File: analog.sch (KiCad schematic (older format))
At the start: 8 parts, among them J18 A3, J19 A4

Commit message: Added images Added information to schematic Added information to layout
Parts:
- renumbered C25 to C21, C26 to C22, J18 to J14, J19 to J15
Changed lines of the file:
@@
 encoding utf-8
 Sheet 8 11
-Title ""
-Date ""
-Rev ""
-Comp ""
-Comment1 ""
+Title "AirMon"
+Date "2020-01-13"
+Rev "0.1"
+Comp "Jörg Bayer"
+Comment1 "CC BY 4.0"
 Comment2 ""
 Comment3 ""
@@
 AR Path="/5E18E639/5E1C5B24" Ref="#PWR?"  Part="1"
 AR Path="/5E1991ED/5E1C5B24" Ref="#PWR?"  Part="1"
-AR Path="/5E1C55BA/5E1C5B24" Ref="#PWR034"  Part="1"
-F 0 "#PWR034" H 6300 1650 50  0001 C CNN
+AR Path="/5E1C55BA/5E1C5B24" Ref="#PWR029"  Part="1"
+F 0 "#PWR029" H 6300 1650 50  0001 C CNN
 F 1 "+5V" H 6315 1973 50  0000 C CNN
 F 2 "" H 6300 1800 50  0001 C CNN
@@
 $EndComp
 $Comp
-L Connector_Generic:Conn_01x03 J18
+L Connector_Generic:Conn_01x03 J14
 U 1 1 5E1C6A01
 P 6600 2100
-F 0 "J18" H 6679 2142 50  0000 L CNN
+F 0 "J14" H 6679 2142 50  0000 L CNN
 F 1 "A3" H 6679 2051 50  0000 L CNN
 F 2 "Connector_PinSocket_2.54mm:PinSocket_1x03_P2.54mm_Vertical" H 6600 2100 50  0001 C CNN
@@
 AR Path="/5E198729/5E1C6A07" Ref="#PWR?"  Part="1"
 AR Path="/5E1991ED/5E1C6A07" Ref="#PWR?"  Part="1"
-AR Path="/5E1C55BA/5E1C6A07" Ref="#PWR035"  Part="1"
-F 0 "#PWR035" H 6300 3050 50  0001 C CNN
+AR Path="/5E1C55BA/5E1C6A07" Ref="#PWR030"  Part="1"
+F 0 "#PWR030" H 6300 3050 50  0001 C CNN
 F 1 "VSS" H 6200 3300 50  0000 C CNN
 F 2 "" H 6300 3200 50  0001 C CNN
@@
 A3
 $Comp
-L Connector_Generic:Conn_01x03 J19
+L Connector_Generic:Conn_01x03 J15
 U 1 1 5E1C6A19
 P 8000 2100
-F 0 "J19" H 8079 2142 50  0000 L CNN
+F 0 "J15" H 8079 2142 50  0000 L CNN
 F 1 "A4" H 8079 2051 50  0000 L CNN
 F 2 "Connector_PinSocket_2.54mm:PinSocket_1x03_P2.54mm_Vertical" H 8000 2100 50  0001 C CNN
@@
 AR Path="/5E198729/5E1C6A1F" Ref="#PWR?"  Part="1"
 AR Path="/5E1991ED/5E1C6A1F" Ref="#PWR?"  Part="1"
-AR Path="/5E1C55BA/5E1C6A1F" Ref="#PWR037"  Part="1"
-F 0 "#PWR037" H 7700 3050 50  0001 C CNN
+AR Path="/5E1C55BA/5E1C6A1F" Ref="#PWR032"  Part="1"
+F 0 "#PWR032" H 7700 3050 50  0001 C CNN
 F 1 "VSS" H 7600 3300 50  0000 C CNN
 F 2 "" H 7700 3200 50  0001 C CNN
@@
 AR Path="/5E18E639/5E1C6CE4" Ref="#PWR?"  Part="1"
 AR Path="/5E1991ED/5E1C6CE4" Ref="#PWR?"  Part="1"
-AR Path="/5E1C55BA/5E1C6CE4" Ref="#PWR036"  Part="1"
-F 0 "#PWR036" H 7700 1650 50  0001 C CNN
+AR Path="/5E1C55BA/5E1C6CE4" Ref="#PWR031"  Part="1"
+F 0 "#PWR031" H 7700 1650 50  0001 C CNN
 F 1 "+5V" H 7715 1973 50  0000 C CNN
 F 2 "" H 7700 1800 50  0001 C CNN
@@
 AR Path="/5E1991ED/5E2B2B40" Ref="C?"  Part="1"
 AR Path="/5E1BB661/5E2B2B40" Ref="C?"  Part="1"
-AR Path="/5E1C55BA/5E2B2B40" Ref="C25"  Part="1"
-F 0 "C25" H 5815 2196 50  0000 L CNN
+AR Path="/5E1C55BA/5E2B2B40" Ref="C21"  Part="1"
+F 0 "C21" H 5815 2196 50  0000 L CNN
 F 1 "1u" H 5815 2105 50  0000 L CNN
 F 2 "Capacitor_SMD:C_0805_2012Metric" H 5738 2000 50  0001 C CNN
@@
 AR Path="/5E1991ED/5E2B5D1A" Ref="C?"  Part="1"
 AR Path="/5E1BB661/5E2B5D1A" Ref="C?"  Part="1"
-AR Path="/5E1C55BA/5E2B5D1A" Ref="C26"  Part="1"
-F 0 "C26" H 7215 2196 50  0000 L CNN
+AR Path="/5E1C55BA/5E2B5D1A" Ref="C22"  Part="1"
+F 0 "C22" H 7215 2196 50  0000 L CNN
 F 1 "1u" H 7215 2105 50  0000 L CNN
 F 2 "Capacitor_SMD:C_0805_2012Metric" H 7138 2000 50  0001 C CNN

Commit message: Added fuse for USB Added buttons for boot and reset Added version number to PCB Changed several component values for improved manufacturing Added BOM Added component position file
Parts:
- C21, C22: lcsc# (none) -> C28323; manf# CL21B105KBFNNNG -> CL21B105KBFNNNE
- R16, R18: lcsc# (none) -> C25819; manf# (none) -> 0603WAF4702T5E
- R17, R19: lcsc# (none) -> C22809; manf# (none) -> 0603WAF1502T5E
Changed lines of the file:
@@
 F 2 "Resistor_SMD:R_0603_1608Metric" V 7330 2350 50  0001 C CNN
 F 3 "~" H 7400 2350 50  0001 C CNN
+F 4 "C25819" H 0   0   50  0001 C CNN "lcsc#"
+F 5 "0603WAF4702T5E" H 0   0   50  0001 C CNN "manf#"
 	1    7400 2350
 	-1   0    0    -1
@@
 F 2 "Resistor_SMD:R_0603_1608Metric" V 7330 2850 50  0001 C CNN
 F 3 "~" H 7400 2850 50  0001 C CNN
+F 4 "C22809" H 0   0   50  0001 C CNN "lcsc#"
+F 5 "0603WAF1502T5E" H 0   0   50  0001 C CNN "manf#"
 	1    7400 2850
 	-1   0    0    -1
@@
 F 2 "Resistor_SMD:R_0603_1608Metric" V 5930 2350 50  0001 C CNN
 F 3 "~" H 6000 2350 50  0001 C CNN
+F 4 "C25819" H 0   0   50  0001 C CNN "lcsc#"
+F 5 "0603WAF4702T5E" H 0   0   50  0001 C CNN "manf#"
 	1    6000 2350
 	-1   0    0    -1
@@
 F 2 "Resistor_SMD:R_0603_1608Metric" V 5930 2850 50  0001 C CNN
 F 3 "~" H 6000 2850 50  0001 C CNN
+F 4 "C22809" H 0   0   50  0001 C CNN "lcsc#"
+F 5 "0603WAF1502T5E" H 0   0   50  0001 C CNN "manf#"
 	1    6000 2850
 	-1   0    0    -1
@@
 F 2 "Capacitor_SMD:C_0805_2012Metric" H 5738 2000 50  0001 C CNN
 F 3 "~" H 5700 2150 50  0001 C CNN
-F 4 "CL21B105KBFNNNG" H 5700 2150 50  0001 C CNN "manf#"
+F 4 "CL21B105KBFNNNE" H 5700 2150 50  0001 C CNN "manf#"
+F 5 "C28323" H 0   0   50  0001 C CNN "lcsc#"
 	1    5700 2150
 	1    0    0    -1
@@
 F 2 "Capacitor_SMD:C_0805_2012Metric" H 7138 2000 50  0001 C CNN
 F 3 "~" H 7100 2150 50  0001 C CNN
-F 4 "CL21B105KBFNNNG" H 7100 2150 50  0001 C CNN "manf#"
+F 4 "CL21B105KBFNNNE" H 7100 2150 50  0001 C CNN "manf#"
+F 5 "C28323" H 0   0   50  0001 C CNN "lcsc#"
 	1    7100 2150
 	1    0    0    -1

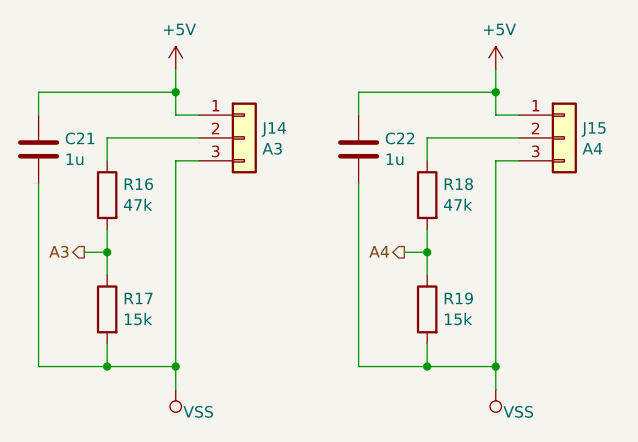
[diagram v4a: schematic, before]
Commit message: Added RFM95 Module for Lora Added Changelog Changed input voltage monitoring from A2(IO35) to A3(IO36) Removed A3 12V compatibility Rearranged IOs to fit new components
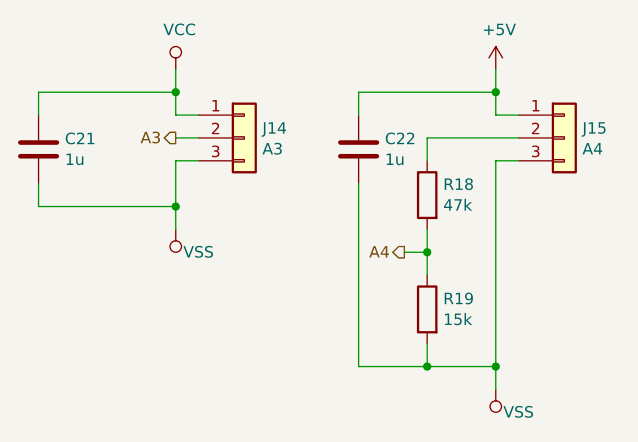
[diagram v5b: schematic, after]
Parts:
- removed R16: 47k, Resistor_SMD:R_0603_1608Metric, symbol Device:R
- removed R17: 15k, Resistor_SMD:R_0603_1608Metric, symbol Device:R
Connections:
- net +5V: no longer C21.1, J14.1 (Pin_1)
- net A3: now also J14.2 (Pin_2)
- new net VCC: C21.1, J14.1 (Pin_1)
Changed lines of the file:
@@
 $Descr A4 11693 8268
 encoding utf-8
-Sheet 8 11
+Sheet 8 12
 Title "AirMon"
 Date "2020-01-17"
@@
 $EndDescr
 $Comp
-L power:+5V #PWR?
-U 1 1 5E1C5B24
-P 6300 1800
-AR Path="/5E18E639/5E1C5B24" Ref="#PWR?"  Part="1"
-AR Path="/5E1991ED/5E1C5B24" Ref="#PWR?"  Part="1"
-AR Path="/5E1C55BA/5E1C5B24" Ref="#PWR029"  Part="1"
-F 0 "#PWR029" H 6300 1650 50  0001 C CNN
-F 1 "+5V" H 6315 1973 50  0000 C CNN
-F 2 "" H 6300 1800 50  0001 C CNN
-F 3 "" H 6300 1800 50  0001 C CNN
-	1    6300 1800
-	1    0    0    -1
-$EndComp
-$Comp
 L Connector_Generic:Conn_01x03 J14
 U 1 1 5E1C6A01
@@
 L power:VSS #PWR?
 U 1 1 5E1C6A07
-P 6300 3200
+P 6300 2500
 AR Path="/5DD6D4DA/5DEBB035/5E1C6A07" Ref="#PWR?"  Part="1"
 AR Path="/5E15DEC3/5E1C6A07" Ref="#PWR?"  Part="1"
@@
 AR Path="/5E1991ED/5E1C6A07" Ref="#PWR?"  Part="1"
 AR Path="/5E1C55BA/5E1C6A07" Ref="#PWR030"  Part="1"
-F 0 "#PWR030" H 6300 3050 50  0001 C CNN
-F 1 "VSS" H 6200 3300 50  0000 C CNN
-F 2 "" H 6300 3200 50  0001 C CNN
-F 3 "" H 6300 3200 50  0001 C CNN
-	1    6300 3200
+F 0 "#PWR030" H 6300 2350 50  0001 C CNN
+F 1 "VSS" H 6200 2600 50  0000 C CNN
+F 2 "" H 6300 2500 50  0001 C CNN
+F 3 "" H 6300 2500 50  0001 C CNN
+	1    6300 2500
 	-1   0    0    1
 $EndComp
@@
 Wire Wire Line
 	6400 2200 6300 2200
-Text HLabel 5900 2600 0    50   Output ~ 0
+Text HLabel 6300 2100 0    50   Output ~ 0
 A3
 $Comp
@@
 Wire Wire Line
 	7400 2500 7400 2600
-$Comp
-L Device:R R?
-U 1 1 5E1C7814
-P 6000 2350
-AR Path="/5DD6D4DA/5DD6D50E/5E1C7814" Ref="R?"  Part="1"
-AR Path="/5DD6D4DA/5DDED058/5E1C7814" Ref="R?"  Part="1"
-AR Path="/5DD6D4DA/5DDED066/5E1C7814" Ref="R?"  Part="1"
-AR Path="/5DD6D4DA/5DDED074/5E1C7814" Ref="R?"  Part="1"
-AR Path="/5DD6D4DA/5DD6D549/5E1C7814" Ref="R?"  Part="1"
-AR Path="/5DD6D4DA/5DDFF593/5E1C7814" Ref="R?"  Part="1"
-AR Path="/5DD6D4DA/5DE2F431/5E1C7814" Ref="R?"  Part="1"
-AR Path="/5E15DEC3/5E1C7814" Ref="R?"  Part="1"
-AR Path="/5E151517/5E1C7814" Ref="R?"  Part="1"
-AR Path="/5E1C55BA/5E1C7814" Ref="R16"  Part="1"
-F 0 "R16" H 5930 2396 50  0000 R CNN
-F 1 "47k" H 5930 2305 50  0000 R CNN
-F 2 "Resistor_SMD:R_0603_1608Metric" V 5930 2350 50  0001 C CNN
-F 3 "~" H 6000 2350 50  0001 C CNN
-F 4 "C25819" H 0   0   50  0001 C CNN "lcsc#"
-F 5 "0603WAF4702T5E" H 0   0   50  0001 C CNN "manf#"
-	1    6000 2350
-	-1   0    0    -1
-$EndComp
-$Comp
-L Device:R R?
-U 1 1 5E1C781A
-P 6000 2850
-AR Path="/5DD6D4DA/5DD6D50E/5E1C781A" Ref="R?"  Part="1"
-AR Path="/5DD6D4DA/5DDED058/5E1C781A" Ref="R?"  Part="1"
-AR Path="/5DD6D4DA/5DDED066/5E1C781A" Ref="R?"  Part="1"
-AR Path="/5DD6D4DA/5DDED074/5E1C781A" Ref="R?"  Part="1"
-AR Path="/5DD6D4DA/5DD6D549/5E1C781A" Ref="R?"  Part="1"
-AR Path="/5DD6D4DA/5DDFF593/5E1C781A" Ref="R?"  Part="1"
-AR Path="/5DD6D4DA/5DE2F431/5E1C781A" Ref="R?"  Part="1"
-AR Path="/5E15DEC3/5E1C781A" Ref="R?"  Part="1"
-AR Path="/5E151517/5E1C781A" Ref="R?"  Part="1"
-AR Path="/5E1C55BA/5E1C781A" Ref="R17"  Part="1"
-F 0 "R17" H 5930 2896 50  0000 R CNN
-F 1 "15k" H 5930 2805 50  0000 R CNN
-F 2 "Resistor_SMD:R_0603_1608Metric" V 5930 2850 50  0001 C CNN
-F 3 "~" H 6000 2850 50  0001 C CNN
-F 4 "C22809" H 0   0   50  0001 C CNN "lcsc#"
-F 5 "0603WAF1502T5E" H 0   0   50  0001 C CNN "manf#"
-	1    6000 2850
-	-1   0    0    -1
-$EndComp
-Wire Wire Line
-	6000 2500 6000 2600
-Wire Wire Line
-	6000 2100 6000 2200
-Wire Wire Line
-	6000 2100 6400 2100
-Wire Wire Line
-	6000 2600 5900 2600
-Connection ~ 6000 2600
-Wire Wire Line
-	6000 2600 6000 2700
+Wire Wire Line
+	6400 2100 6300 2100
 Wire Wire Line
 	7400 2200 7400 2100
@@
 Wire Wire Line
 	7700 3100 7700 3200
-Wire Wire Line
-	6300 3100 6000 3100
-Wire Wire Line
-	6000 3100 6000 3000
-Connection ~ 6300 3100
-Wire Wire Line
-	6300 3100 6300 3200
+Connection ~ 6300 2400
+Wire Wire Line
+	6300 2400 6300 2500
 $Comp
 L Device:C C?
@@
 	6300 1900 6300 1800
 Wire Wire Line
-	6300 2200 6300 3100
-Wire Wire Line
-	6000 3100 5700 3100
-Wire Wire Line
-	5700 3100 5700 2300
-Connection ~ 6000 3100
+	6300 2200 6300 2400
+Wire Wire Line
+	5700 2400 5700 2300
 $Comp
 L Device:C C?
@@
 Wire Wire Line
 	7700 1900 7700 1800
+Wire Wire Line
+	5700 2400 6300 2400
+$Comp
+L power:VCC #PWR?
+U 1 1 5E313941
+P 6300 1800
+AR Path="/5DD6D4DA/5DEBB035/5E313941" Ref="#PWR?"  Part="1"
+AR Path="/5E15DEC3/5E313941" Ref="#PWR?"  Part="1"
+AR Path="/5E151517/5E313941" Ref="#PWR?"  Part="1"
+AR Path="/5E1961BA/5E313941" Ref="#PWR?"  Part="1"
+AR Path="/5E198729/5E313941" Ref="#PWR?"  Part="1"
+AR Path="/5E1C55BA/5E313941" Ref="#PWR029"  Part="1"
+AR Path="/5E1CBADF/5E313941" Ref="#PWR?"  Part="1"
+F 0 "#PWR029" H 6300 1650 50  0001 C CNN
+F 1 "VCC" H 6317 1973 50  0000 C CNN
+F 2 "" H 6300 1800 50  0001 C CNN
+F 3 "" H 6300 1800 50  0001 C CNN
+	1    6300 1800
+	1    0    0    -1
+$EndComp
 $EndSCHEMATC
